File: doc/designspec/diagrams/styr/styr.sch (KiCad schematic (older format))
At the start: 7 parts

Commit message: fix styrmodule
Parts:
- added CAP: 100nF, symbol Device:C_Small
- U?: symbol MCU_Microchip_ATmega:ATmega1284P-PU -> styr-rescue:ATmega1284P-PU-MCU_Microchip_ATmega
- U?: symbol exo3:IQEXO-3 -> styr-rescue:IQEXO-3-exo3
- _?: symbol jma162a:JMA162A -> styr-rescue:JMA162A-jma162a
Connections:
- wire segments 41 -> 56
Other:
- note added: "0->0, 1->1, 2->2, 3->3, 4->4, 5->5, 6->6"
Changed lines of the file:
@@
 $EndComp
 $Comp
-L MCU_Microchip_ATmega:ATmega1284P-PU U?
+L styr-rescue:ATmega1284P-PU-MCU_Microchip_ATmega U?
 U 1 1 5BEA84E2
 P 2850 3150
@@
 $EndComp
 $Comp
-L exo3:IQEXO-3 U?
+L styr-rescue:IQEXO-3-exo3 U?
 U 1 1 5BEB103D
 P 1350 2150
@@
 SS
 $Comp
-L jma162a:JMA162A _?
+L styr-rescue:JMA162A-jma162a _?
 U 1 1 5BEDF369
-P 6650 3250
-F 0 "_?" V 6450 2900 50  0001 C CNN
-F 1 "JMA162A" H 6650 2675 50  0000 C CNN
-F 2 "Display_7Segment:DA04-11SYKWA" V 7825 3225 50  0001 C CNN
-F 3 "http://www.kingbright.com/attachments/file/psearch/000/00/00/DA04-11SYKWA(Ver.6A).pdf" V 6450 3670 50  0001 C CNN
-	1    6650 3250
-	0    1    -1   0
-$EndComp
-Wire Wire Line
-	6400 2550 6400 2150
-Wire Wire Line
-	6400 2150 3450 2150
-Wire Wire Line
-	6500 2550 6500 2050
-Wire Wire Line
-	6500 2050 3450 2050
-Wire Wire Line
-	6600 2550 6600 1950
-Wire Wire Line
-	6600 1950 3450 1950
-Wire Wire Line
-	6700 2550 6700 1850
-Wire Wire Line
-	6700 1850 3450 1850
-Wire Wire Line
-	6800 2550 6800 1750
-Wire Wire Line
-	6800 1750 3450 1750
-Wire Wire Line
-	6900 2550 6900 1650
-Wire Wire Line
-	6900 1650 3450 1650
-Wire Wire Line
-	3450 1550 7000 1550
-Wire Wire Line
-	7000 1550 7000 2550
-Wire Wire Line
-	7100 2550 7100 1450
-Wire Wire Line
-	7100 1450 3450 1450
-Wire Wire Line
-	3450 2350 6300 2350
-Wire Wire Line
-	6300 2350 6300 2550
+P 6800 2300
+F 0 "_?" V 6600 1950 50  0001 C CNN
+F 1 "JMA162A" H 6800 1725 50  0000 C CNN
+F 2 "Display_7Segment:DA04-11SYKWA" V 7975 2275 50  0001 C CNN
+F 3 "http://www.kingbright.com/attachments/file/psearch/000/00/00/DA04-11SYKWA(Ver.6A).pdf" V 6600 2720 50  0001 C CNN
+	1    6800 2300
+	0    -1   -1   0
+$EndComp
 Wire Wire Line
 	3450 4650 4150 4650
@@
 L power:GNDREF #PWR?
 U 1 1 5BEEFE97
-P 6300 3950
-F 0 "#PWR?" H 6300 3700 50  0001 C CNN
-F 1 "GNDREF" H 6305 3777 50  0000 C CNN
-F 2 "" H 6300 3950 50  0001 C CNN
-F 3 "" H 6300 3950 50  0001 C CNN
-	1    6300 3950
+P 7150 3000
+F 0 "#PWR?" H 7150 2750 50  0001 C CNN
+F 1 "GNDREF" H 7155 2827 50  0000 C CNN
+F 2 "" H 7150 3000 50  0001 C CNN
+F 3 "" H 7150 3000 50  0001 C CNN
+	1    7150 3000
 	1    0    0    -1
 $EndComp
@@
 L power:+5V #PWR?
 U 1 1 5BE1138F
-P 7250 3500
-F 0 "#PWR?" H 7250 3350 50  0001 C CNN
-F 1 "+5V" H 7265 3673 50  0000 C CNN
-F 2 "" H 7250 3500 50  0001 C CNN
-F 3 "" H 7250 3500 50  0001 C CNN
-	1    7250 3500
-	0    1    1    0
+P 6200 2650
+F 0 "#PWR?" H 6200 2500 50  0001 C CNN
+F 1 "+5V" H 6215 2823 50  0000 C CNN
+F 2 "" H 6200 2650 50  0001 C CNN
+F 3 "" H 6200 2650 50  0001 C CNN
+	1    6200 2650
+	0    -1   -1   0
 $EndComp
 $Comp
@@
 Wire Wire Line
 	2850 1150 2850 1000
-Wire Wire Line
-	2850 1000 2900 1000
-Wire Wire Line
-	2950 1000 2950 1150
 $Comp
 L power:+5V #PWR?
 U 1 1 5BE15085
-P 2900 1000
-F 0 "#PWR?" H 2900 850 50  0001 C CNN
-F 1 "+5V" H 2915 1173 50  0000 C CNN
-F 2 "" H 2900 1000 50  0001 C CNN
-F 3 "" H 2900 1000 50  0001 C CNN
-	1    2900 1000
-	1    0    0    -1
-$EndComp
-Connection ~ 2900 1000
-Wire Wire Line
-	2900 1000 2950 1000
+P 2950 800
+F 0 "#PWR?" H 2950 650 50  0001 C CNN
+F 1 "+5V" H 2965 973 50  0000 C CNN
+F 2 "" H 2950 800 50  0001 C CNN
+F 3 "" H 2950 800 50  0001 C CNN
+	1    2950 800
+	0    1    1    0
+$EndComp
 $Comp
 L Analog_Switch:ADG417BN U?
@@
 Text Label 4150 4550 0    50   ~ 0
 PWM_MOTOR
+$Comp
+L power:GNDREF #PWR?
+U 1 1 5BE49225
+P 7050 1450
+F 0 "#PWR?" H 7050 1200 50  0001 C CNN
+F 1 "GNDREF" H 7055 1277 50  0000 C CNN
+F 2 "" H 7050 1450 50  0001 C CNN
+F 3 "" H 7050 1450 50  0001 C CNN
+	1    7050 1450
+	-1   0    0    1
+$EndComp
+Wire Wire Line
+	3550 1450 3550 1550
+Wire Wire Line
+	3550 1550 3450 1550
+Connection ~ 3550 1450
+Wire Wire Line
+	3550 1450 3450 1450
+Wire Wire Line
+	3550 1550 3550 1650
+Wire Wire Line
+	3550 1650 3450 1650
+Connection ~ 3550 1550
+Wire Wire Line
+	3550 1650 3550 1750
+Wire Wire Line
+	3550 1750 3450 1750
+Connection ~ 3550 1650
+Wire Wire Line
+	3550 1750 3550 1850
+Wire Wire Line
+	3550 1850 3450 1850
+Connection ~ 3550 1750
+Wire Wire Line
+	3550 1850 3550 1950
+Wire Wire Line
+	3550 1950 3450 1950
+Connection ~ 3550 1850
+Wire Wire Line
+	3550 1950 3550 2050
+Wire Wire Line
+	3550 2050 3450 2050
+Connection ~ 3550 1950
+Text Notes 4150 1450 0    50   ~ 0
+0->0, 1->1, 2->2, 3->3, 4->4, 5->5, 6->6
+Wire Wire Line
+	7050 1450 7050 1600
+Wire Wire Line
+	6950 1450 6950 1600
+Wire Wire Line
+	6850 1450 6850 1600
+Wire Wire Line
+	6750 1450 6750 1600
+Wire Wire Line
+	6650 1450 6650 1600
+Wire Wire Line
+	6550 1450 6550 1600
+Wire Wire Line
+	6450 1450 6450 1600
+Wire Wire Line
+	6350 1450 6350 1600
+Connection ~ 6350 1450
+Wire Wire Line
+	6450 1450 6550 1450
+Connection ~ 6450 1450
+Connection ~ 6550 1450
+Wire Wire Line
+	6550 1450 6650 1450
+Wire Wire Line
+	6650 1450 6750 1450
+Connection ~ 6650 1450
+Connection ~ 6750 1450
+Wire Wire Line
+	6750 1450 6850 1450
+Wire Wire Line
+	6850 1450 6950 1450
+Connection ~ 6850 1450
+Wire Wire Line
+	6350 1450 6450 1450
+Wire Wire Line
+	3550 1450 6350 1450
+Wire Wire Line
+	6200 2450 3450 2450
+Wire Wire Line
+	7150 1600 7150 1550
+Wire Wire Line
+	7150 1550 4950 1550
+Wire Wire Line
+	4950 1550 4950 2350
+Wire Wire Line
+	4950 2350 3450 2350
+$Comp
+L Device:C_Small CAP
+U 1 1 5BE63E89
+P 2850 800
+F 0 "CAP" V 2621 800 50  0000 C CNN
+F 1 "100nF" V 2712 800 50  0000 C CNN
+F 2 "" H 2850 800 50  0001 C CNN
+F 3 "~" H 2850 800 50  0001 C CNN
+	1    2850 800
+	0    1    1    0
+$EndComp
+Wire Wire Line
+	2950 800  2950 1000
+Connection ~ 2950 800
+Wire Wire Line
+	2950 1000 2850 1000
+Connection ~ 2950 1000
+Wire Wire Line
+	2950 1000 2950 1150
+$Comp
+L power:GNDREF #PWR?
+U 1 1 5BE6A65E
+P 2750 800
+F 0 "#PWR?" H 2750 550 50  0001 C CNN
+F 1 "GNDREF" H 2755 627 50  0000 C CNN
+F 2 "" H 2750 800 50  0001 C CNN
+F 3 "" H 2750 800 50  0001 C CNN
+	1    2750 800
+	0    1    1    0
+$EndComp
 $EndSCHEMATC

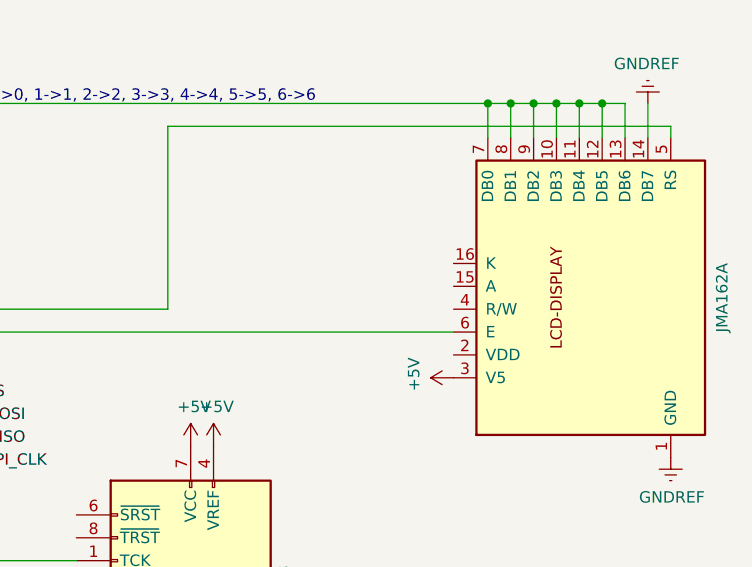
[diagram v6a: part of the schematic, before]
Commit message: add gnd on r/w
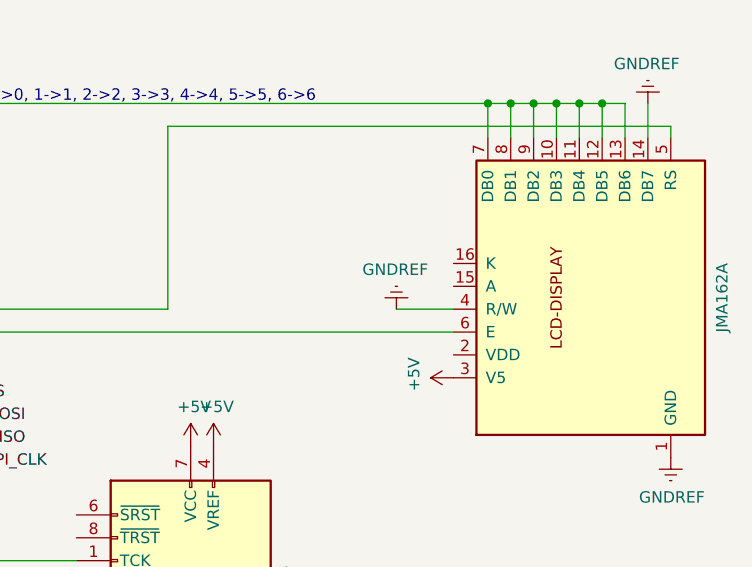
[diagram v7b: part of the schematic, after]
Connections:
- net GNDREF: now also _?.4 (R/W)
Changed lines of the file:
@@
 	0    1    1    0
 $EndComp
+$Comp
+L power:GNDREF #PWR?
+U 1 1 5BE45184
+P 5950 2350
+F 0 "#PWR?" H 5950 2100 50  0001 C CNN
+F 1 "GNDREF" H 5955 2177 50  0000 C CNN
+F 2 "" H 5950 2350 50  0001 C CNN
+F 3 "" H 5950 2350 50  0001 C CNN
+	1    5950 2350
+	-1   0    0    1
+$EndComp
+Wire Wire Line
+	5950 2350 6200 2350
 $EndSCHEMATC
